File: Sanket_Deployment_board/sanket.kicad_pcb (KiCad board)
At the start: 2 copper layers, 95.9 x 92 mm, 42 parts, among them J2 Conn_02x03_Counter_Clockwise, J3 Conn_02x03_Counter_Clockwise, U1 SN74LVC1G17QDCKRQ1

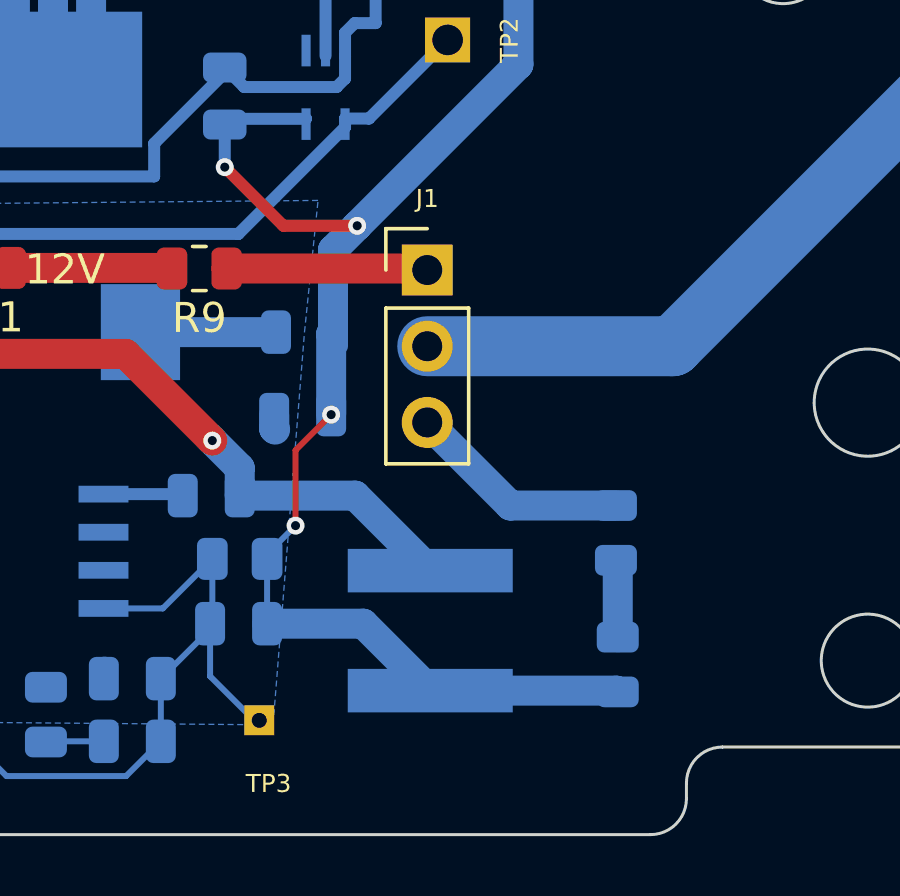
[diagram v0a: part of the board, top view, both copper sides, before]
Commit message: In the main board, branching power at 3V3 to burn elements after decoupling capacitors, power trace branched earlier before
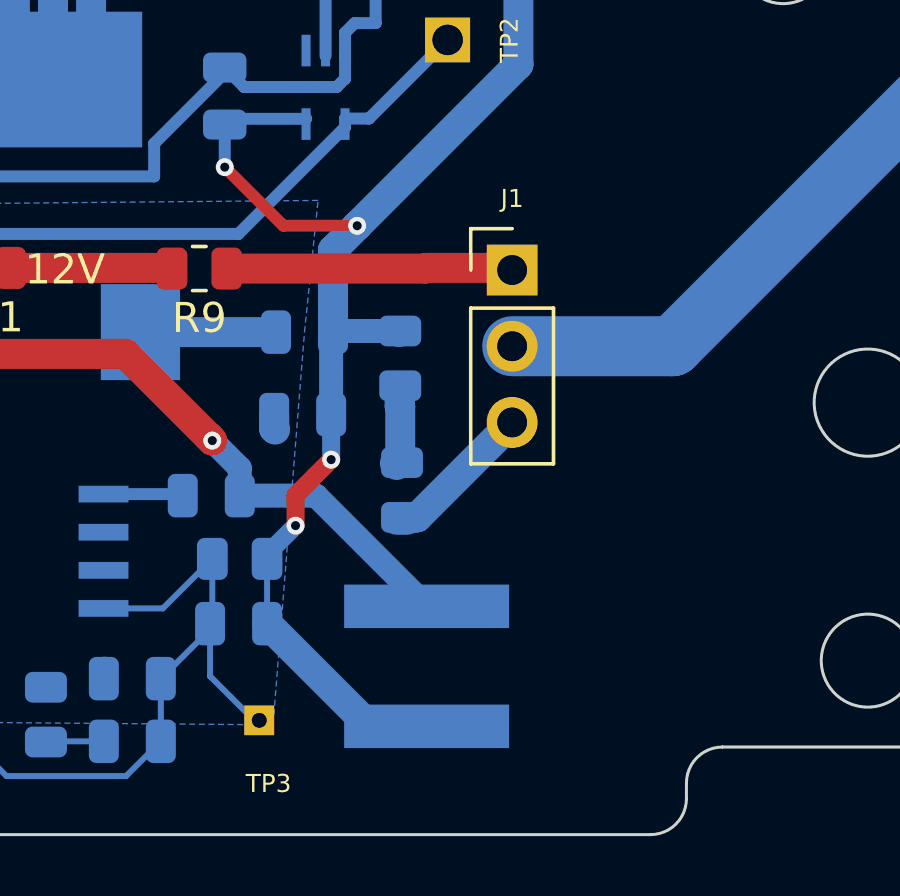
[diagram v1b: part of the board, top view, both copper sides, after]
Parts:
- moved R12 12.5 mm to (128.8, 133.4), turned to -90 degrees
- moved R10 7.27 mm to (128.8, 137.8), turned to 90 degrees
- moved J1 2.83 mm to (132.5, 130.5)
- moved L1 1.20 mm to (129.6, 143.7)
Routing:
- net +3V3: track 97.5 -> 94.1 mm
- net Net-(J1-Pin_1): track 6.71 -> 9.55 mm
- net /BurnWire1IN: track 84.9 -> 82.1 mm
- net Net-(J1-Pin_3): track 7.44 -> 5.33 mm
